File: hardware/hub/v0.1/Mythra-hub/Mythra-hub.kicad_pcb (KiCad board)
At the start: 6 copper layers, 110 x 81 mm, 55 parts, among them J1 918-418K2022C40000, J2 Molex Power Input, J3 918-418K2022C40000, J4 918-418K2022C40000, J5 918-418K2022C40000, J6 918-418K2022C40000, U1 TUSB8042A, U2 HD3SS460, U3 BD95861MUV, Y1 24MHz

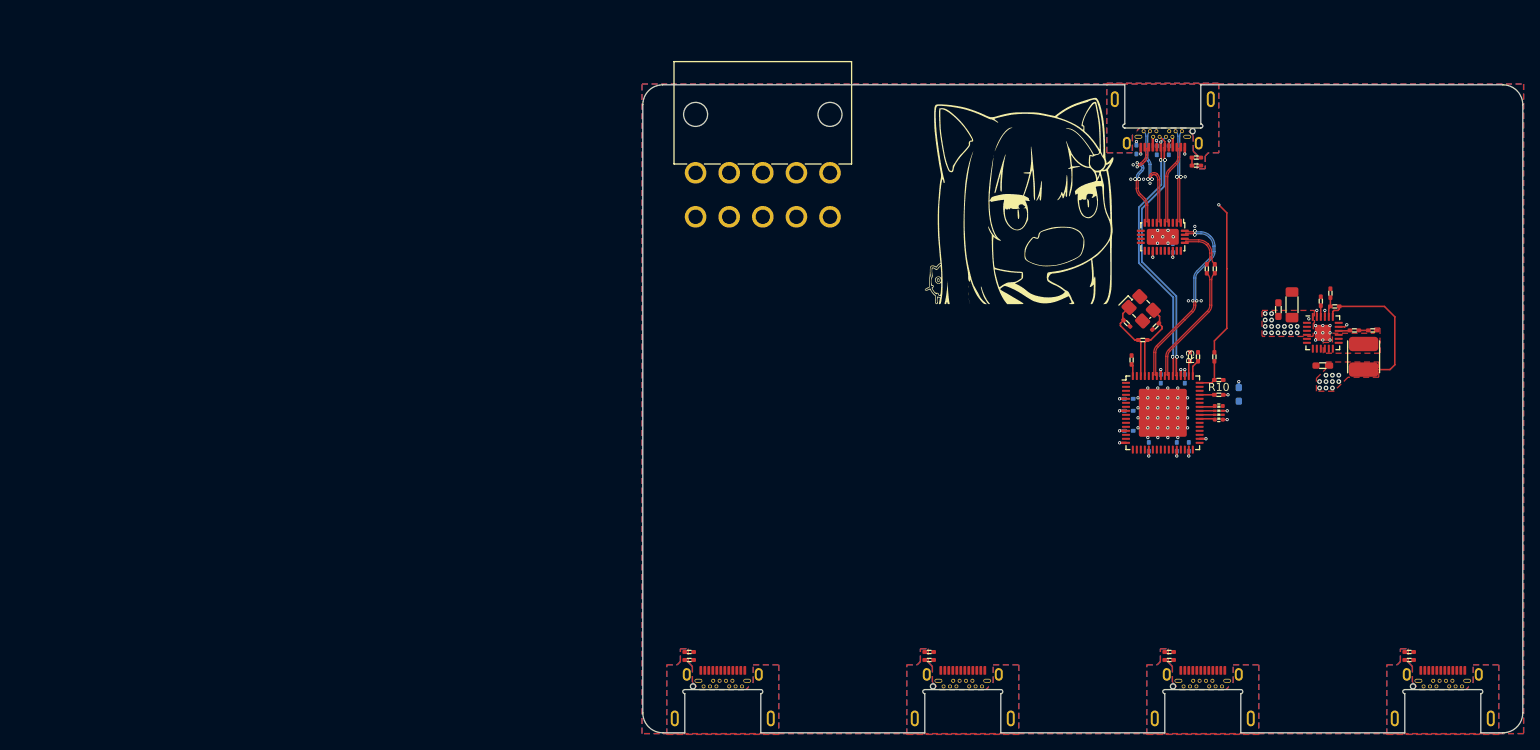
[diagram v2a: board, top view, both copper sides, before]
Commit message: Begun laying out the new power supplies and the crosspoints for the DFPs
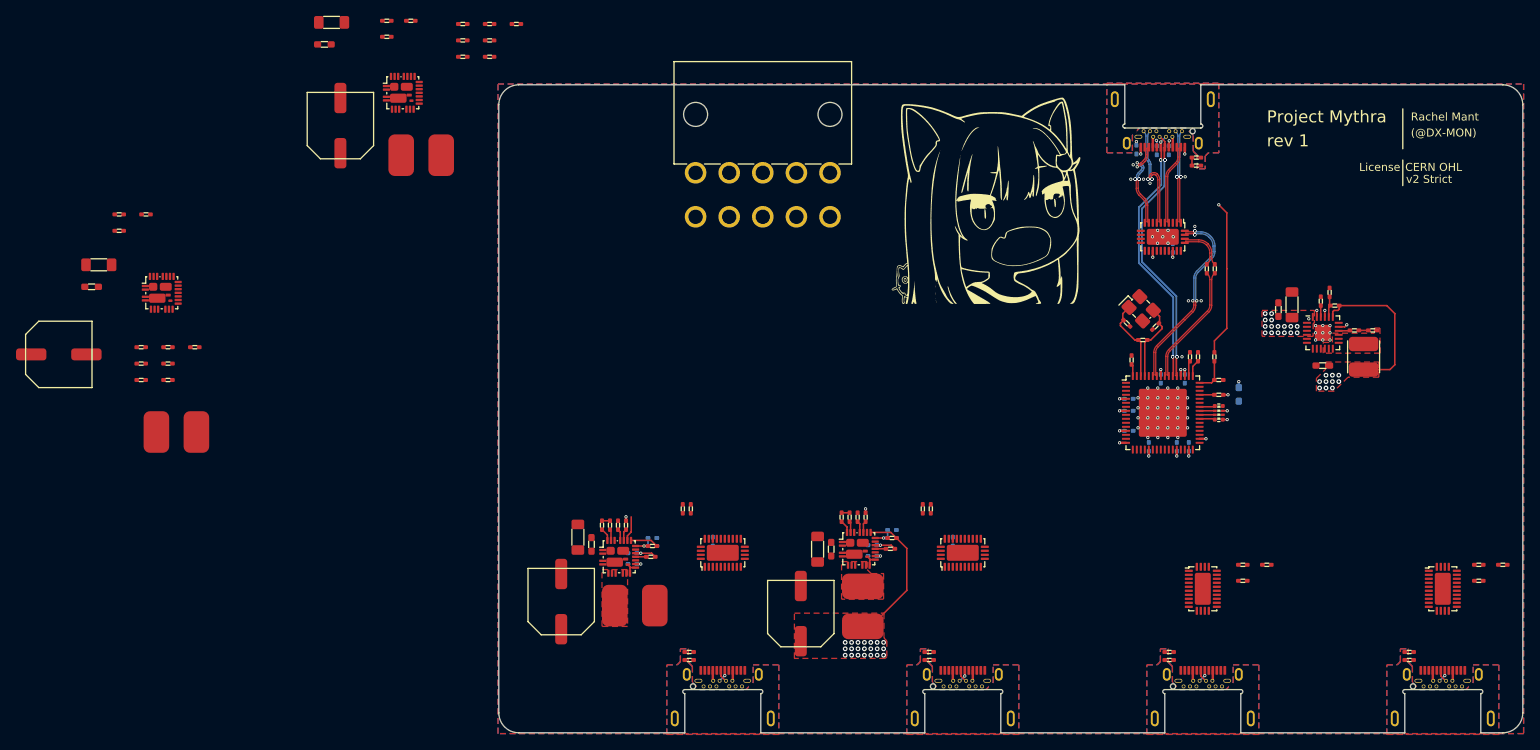
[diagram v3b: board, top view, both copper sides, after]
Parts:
- added C27: 0.1uF, rhais_rcl:C0402, F.Cu at (90.0, 112.0)
- added C28: 0.1uF, rhais_rcl:C0402, F.Cu at (91.0, 112.0)
- added C29: 0.1uF, rhais_rcl:C0402, B.Cu at (93.8, 116.1)
- added C30: 0.1uF, rhais_rcl:C0402, F.Cu at (120.0, 112.0)
- added C31: 0.1uF, rhais_rcl:C0402, F.Cu at (121.0, 112.0)
- added C32: 0.1uF, rhais_rcl:C0402, B.Cu at (123.8, 116.1)
- added C33: 0.1uF, rhais_rcl:C0402, F.Cu at (160.0, 121.0)
- added C34: 0.1uF, rhais_rcl:C0402, F.Cu at (160.0, 119.0)
- added C35: 0.1uF, rhais_rcl:C0402, F.Cu at (163.0, 119.0)
- added C36: 0.1uF, rhais_rcl:C0402, F.Cu at (189.5, 121.0)
- added C37: 0.1uF, rhais_rcl:C0402, F.Cu at (189.5, 119.0)
- added C38: 0.1uF, rhais_rcl:C0402, F.Cu at (192.5, 119.0)
- added C39: 1uF, rhais_rcl:C0402, B.Cu at (83.7, 117.5)
- added C40: 2.2uF, rhais_rcl:C0402, B.Cu at (83.7, 118.9)
- added C41: 0.1uF, rhais_rcl:C0402, F.Cu at (80.9, 114.0)
- added C42: 1uF, rhais_rcl:C0402, B.Cu at (113.7, 116.5)
- added C43: 2.2uF, rhais_rcl:C0402, B.Cu at (113.7, 117.9)
- added C44: 0.1uF, rhais_rcl:C0402, F.Cu at (110.8, 113.0)
- added C45: 1uF, rhais_rcl:C0402, F.Cu at (62.5, 51.4)
- added C46: 2.2uF, rhais_rcl:C0402, F.Cu at (62.5, 53.5)
- added C47: 0.1uF, rhais_rcl:C0402, F.Cu at (56.0, 51.0)
- added C48: 1uF, rhais_rcl:C0402, F.Cu at (22.3, 91.8)
- added C49: 2.2uF, rhais_rcl:C0402, F.Cu at (22.3, 93.8)
- added C50: 0.1uF, rhais_rcl:C0402, F.Cu at (22.9, 75.2)
- added C51: 47uF, rhais_rcl:C_Elec_8.3x8.3mm, F.Cu at (74.8, 123.6)
- added C52: 47uF, rhais_rcl:C_Elec_8.3x8.3mm, F.Cu at (104.8, 125.1)
- added C53: 47uF, rhais_rcl:C_Elec_8.3x8.3mm, F.Cu at (47.2, 64.1)
- added C54: 47uF, rhais_rcl:C_Elec_8.3x8.3mm, F.Cu at (12.0, 92.7)
- added C55: 10uF, rhais_rcl:C1206, F.Cu at (76.9, 115.5)
- added C56: 1uF, rhais_rcl:C0603, F.Cu at (78.6, 116.5)
- added C57: 10uF, rhais_rcl:C1206, F.Cu at (106.8, 117.0)
- added C58: 1uF, rhais_rcl:C0603, F.Cu at (108.5, 117.0)
- added C59: 10uF, rhais_rcl:C1206, F.Cu at (46.1, 51.2)
- added C60: 1uF, rhais_rcl:C0603, F.Cu at (45.2, 54.0)
- added C61: 10uF, rhais_rcl:C1206, F.Cu at (17.0, 81.5)
- added C62: 1uF, rhais_rcl:C0603, F.Cu at (16.1, 84.2)
- added L2: 6.3µH, rhais_bourns:SRN6045TA, F.Cu at (84.0, 124.1)
- added L3: 6.3µH, rhais_bourns:SRN6045TA, F.Cu at (112.5, 124.2)
- added L4: 6.3µH, rhais_bourns:SRN6045TA, F.Cu at (57.3, 67.8)
- added L5: 6.3µH, rhais_bourns:SRN6045TA, F.Cu at (26.7, 102.4)
- added R18: 200k, rhais_rcl:R0402, F.Cu at (81.9, 114.0)
- added R19: 51k, rhais_rcl:R0402, F.Cu at (82.9, 114.0)
- added R20: 2R2, rhais_rcl:R0402, F.Cu at (79.9, 114.0)
- added R21: 10k, rhais_rcl:R0402, F.Cu at (86.0, 118.0)
- added R22: 36.7k, rhais_rcl:R0402, F.Cu at (86.2, 116.7)
- added R23: 14k, rhais_rcl:R0402, B.Cu at (86.2, 115.7)
- added R24: 2.3k, rhais_rcl:R0402, B.Cu at (86.2, 116.7)
- added R25: 200k, rhais_rcl:R0402, F.Cu at (111.8, 113.0)
- added R26: 51k, rhais_rcl:R0402, F.Cu at (112.8, 113.0)
- added R27: 2R2, rhais_rcl:R0402, F.Cu at (109.8, 113.0)
- added R28: 10k, rhais_rcl:R0402, F.Cu at (116.0, 117.0)
- added R29: 36.7k, rhais_rcl:R0402, F.Cu at (116.2, 115.7)
- added R30: 14k, rhais_rcl:R0402, B.Cu at (116.2, 114.7)
- added R31: 2.3k, rhais_rcl:R0402, B.Cu at (116.2, 115.7)
- added R32: 200k, rhais_rcl:R0402, F.Cu at (69.2, 51.4)
- added R33: 51k, rhais_rcl:R0402, F.Cu at (62.5, 55.5)
- added R34: 2R2, rhais_rcl:R0402, F.Cu at (53.0, 53.0)
- added R35: 10k, rhais_rcl:R0402, F.Cu at (53.0, 51.0)
- added R36: 36.7k, rhais_rcl:R0402, F.Cu at (65.8, 51.4)
- added R37: 14k, rhais_rcl:R0402, F.Cu at (65.8, 55.5)
- added R38: 2.3k, rhais_rcl:R0402, F.Cu at (65.8, 53.5)
- added R39: 200k, rhais_rcl:R0402, F.Cu at (29.0, 91.8)
- added R40: 51k, rhais_rcl:R0402, F.Cu at (22.3, 95.9)
- added R41: 2R2, rhais_rcl:R0402, F.Cu at (19.6, 77.2)
- added R42: 10k, rhais_rcl:R0402, F.Cu at (19.6, 75.2)
- added R43: 36.7k, rhais_rcl:R0402, F.Cu at (25.6, 91.8)
- added R44: 14k, rhais_rcl:R0402, F.Cu at (25.6, 95.9)
- added R45: 2.3k, rhais_rcl:R0402, F.Cu at (25.6, 93.8)
- added U10: SiC437/8, rhais_package-vishay:MLP44-24L, F.Cu at (55.0, 60.0)
- added U11: SiC437/8, rhais_package-vishay:MLP44-24L, F.Cu at (24.9, 85.0)
- added U4: HD3SS460, rhais_package-qfn:WQFN-28-1EP_3.5x5.5_P0.5mm_EP2x4mm, F.Cu at (95.0, 117.5)
- added U5: HD3SS460, rhais_package-qfn:WQFN-28-1EP_3.5x5.5_P0.5mm_EP2x4mm, F.Cu at (125.0, 117.5)
- added U6: HD3SS460, rhais_package-qfn:WQFN-28-1EP_3.5x5.5_P0.5mm_EP2x4mm, F.Cu at (155.0, 122.0)
- added U7: HD3SS460, rhais_package-qfn:WQFN-28-1EP_3.5x5.5_P0.5mm_EP2x4mm, F.Cu at (185.0, 122.0)
- added U8: SiC437/8, rhais_package-vishay:MLP44-24L, F.Cu at (82.0, 118.0)
- added U9: SiC437/8, rhais_package-vishay:MLP44-24L, F.Cu at (112.0, 117.0)
- moved G*** 4.15 mm to (128.6, 73.3)
- moved R12 0.14 mm to (170.8, 85.0)
- moved R11 0.10 mm to (171.5, 86.6)
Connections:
- net /UFP/UP_RX+ renamed /UFP/UFP_RX+
- net /UFP/UP_RX- renamed /UFP/UFP_RX-
- net /UFP/UP_RX1+ renamed /UFP/UFP_RX1+
- net /UFP/UP_RX1- renamed /UFP/UFP_RX1-
- net /UFP/UP_RX2+ renamed /UFP/UFP_RX2+
- net /UFP/UP_RX2- renamed /UFP/UFP_RX2-
- net /UFP/UP_TX+ renamed /UFP/UFP_TX+
- net /UFP/UP_TX- renamed /UFP/UFP_TX-
- net /UFP/UP_TX1+ renamed /UFP/UFP_TX1+
- net /UFP/UP_TX1- renamed /UFP/UFP_TX1-
- net /UFP/UP_TX2+ renamed /UFP/UFP_TX2+
- net /UFP/UP_TX2- renamed /UFP/UFP_TX2-
- net /UFP/UP_TXC+ renamed /UFP/UFP_TXC+
- net /UFP/UP_TXC- renamed /UFP/UFP_TXC-
- net Net-(J3-PadA4) renamed /DFP1/DFP_VBUS
- net Net-(J4-PadA4) renamed /DFP2/DFP_VBUS
- net Net-(J5-PadA4) renamed /DFP3/DFP_VBUS
- net Net-(J6-PadA4) renamed /DFP4/DFP_VBUS
- J3 pad A10: unconnected-(J3-PadA10) -> /DFP1/DFP_RX2-
- J3 pad A11: unconnected-(J3-PadA11) -> /DFP1/DFP_RX2+
- J3 pad A2: unconnected-(J3-PadA2) -> /DFP1/DFP_TX1+
- J3 pad A3: unconnected-(J3-PadA3) -> /DFP1/DFP_TX1-
- J3 pad B10: unconnected-(J3-PadB10) -> /DFP1/DFP_RX1-
- J3 pad B11: unconnected-(J3-PadB11) -> /DFP1/DFP_RX1+
- J3 pad B2: unconnected-(J3-PadB2) -> /DFP1/DFP_TX2+
- J3 pad B3: unconnected-(J3-PadB3) -> /DFP1/DFP_TX2-
- J4 pad A10: unconnected-(J4-PadA10) -> /DFP2/DFP_RX2-
- J4 pad A11: unconnected-(J4-PadA11) -> /DFP2/DFP_RX2+
- J4 pad A2: unconnected-(J4-PadA2) -> /DFP2/DFP_TX1+
- J4 pad A3: unconnected-(J4-PadA3) -> /DFP2/DFP_TX1-
- J4 pad B10: unconnected-(J4-PadB10) -> /DFP2/DFP_RX1-
- J4 pad B11: unconnected-(J4-PadB11) -> /DFP2/DFP_RX1+
- J4 pad B2: unconnected-(J4-PadB2) -> /DFP2/DFP_TX2+
- J4 pad B3: unconnected-(J4-PadB3) -> /DFP2/DFP_TX2-
- J5 pad A10: unconnected-(J5-PadA10) -> /DFP3/DFP_RX2-
- J5 pad A11: unconnected-(J5-PadA11) -> /DFP3/DFP_RX2+
- J5 pad A2: unconnected-(J5-PadA2) -> /DFP3/DFP_TX1+
- J5 pad A3: unconnected-(J5-PadA3) -> /DFP3/DFP_TX1-
- J5 pad B10: unconnected-(J5-PadB10) -> /DFP3/DFP_RX1-
- J5 pad B11: unconnected-(J5-PadB11) -> /DFP3/DFP_RX1+
- J5 pad B2: unconnected-(J5-PadB2) -> /DFP3/DFP_TX2+
- J5 pad B3: unconnected-(J5-PadB3) -> /DFP3/DFP_TX2-
- J6 pad A10: unconnected-(J6-PadA10) -> /DFP4/DFP_RX2-
- J6 pad A11: unconnected-(J6-PadA11) -> /DFP4/DFP_RX2+
- J6 pad A2: unconnected-(J6-PadA2) -> /DFP4/DFP_TX1+
- J6 pad A3: unconnected-(J6-PadA3) -> /DFP4/DFP_TX1-
- J6 pad B10: unconnected-(J6-PadB10) -> /DFP4/DFP_RX1-
- J6 pad B11: unconnected-(J6-PadB11) -> /DFP4/DFP_RX1+
- J6 pad B2: unconnected-(J6-PadB2) -> /DFP4/DFP_TX2+
- J6 pad B3: unconnected-(J6-PadB3) -> /DFP4/DFP_TX2-
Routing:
- net /DFP2/DFP_VBUS: track 0.00 -> 20.6 mm, vias 0 -> 21
- net /DFP1/DFP_SMPS_VDD: track 0.00 -> 8.92 mm, vias 0 -> 2
- net /DFP2/DFP_SMPS_VDD: track 0.00 -> 8.87 mm, vias 0 -> 2
- net /DFP1/DFP_VBUS: track 0.00 -> 6.16 mm
- net /DFP1/DFP_SMPS_EN: track 0.00 -> 3.15 mm
- net Net-(R22-Pad2): track 0.00 -> 3.05 mm, vias 0 -> 1
- net Net-(R29-Pad2): track 0.00 -> 3.05 mm, vias 0 -> 1
- net /DFP4/DFP_VBUS: track 0.00 -> 2.64 mm
- net /DFP3/DFP_VBUS: track 0.00 -> 2.64 mm
- net unconnected-(U9-Pad10): track 0.00 -> 1.87 mm
- net unconnected-(U8-Pad10): track 0.00 -> 1.87 mm
- net Net-(R27-Pad1): track 0.00 -> 1.63 mm
- net Net-(R20-Pad1): track 0.00 -> 1.63 mm
- net /DFP4/DFP_D+: track 0.00 -> 1.60 mm
- net /DFP3/DFP_D+: track 0.00 -> 1.60 mm
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- added copper zone on In3.Cu, net +5V
- added copper zone on F.Cu, net /DFP1/DFP_SMPS_SW
- added copper zone on F.Cu, net /DFP2/DFP_SMPS_SW
- added copper zone on F.Cu, net /DFP2/DFP_VBUS
- added copper zone on In2.Cu, net /DFP2/DFP_VBUS
- added copper zone on In3.Cu, net /DFP2/DFP_VBUS
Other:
- board size 110 x 81 mm -> 128 x 81 mm
- board text added: "(@DX-MON)"
- board text added: "CERN OHL"
- board text added: "License"
- board text added: "Project Mythra"
- board text added: "Rachel Mant"
- board text added: "rev 1"
- board text added: "v2 Strict"
